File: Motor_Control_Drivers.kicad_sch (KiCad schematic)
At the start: 4 parts, among them J1101 SEI-125-02-GF-S-M-AT, J1102 SEI-115-02-GF-S-M-AT

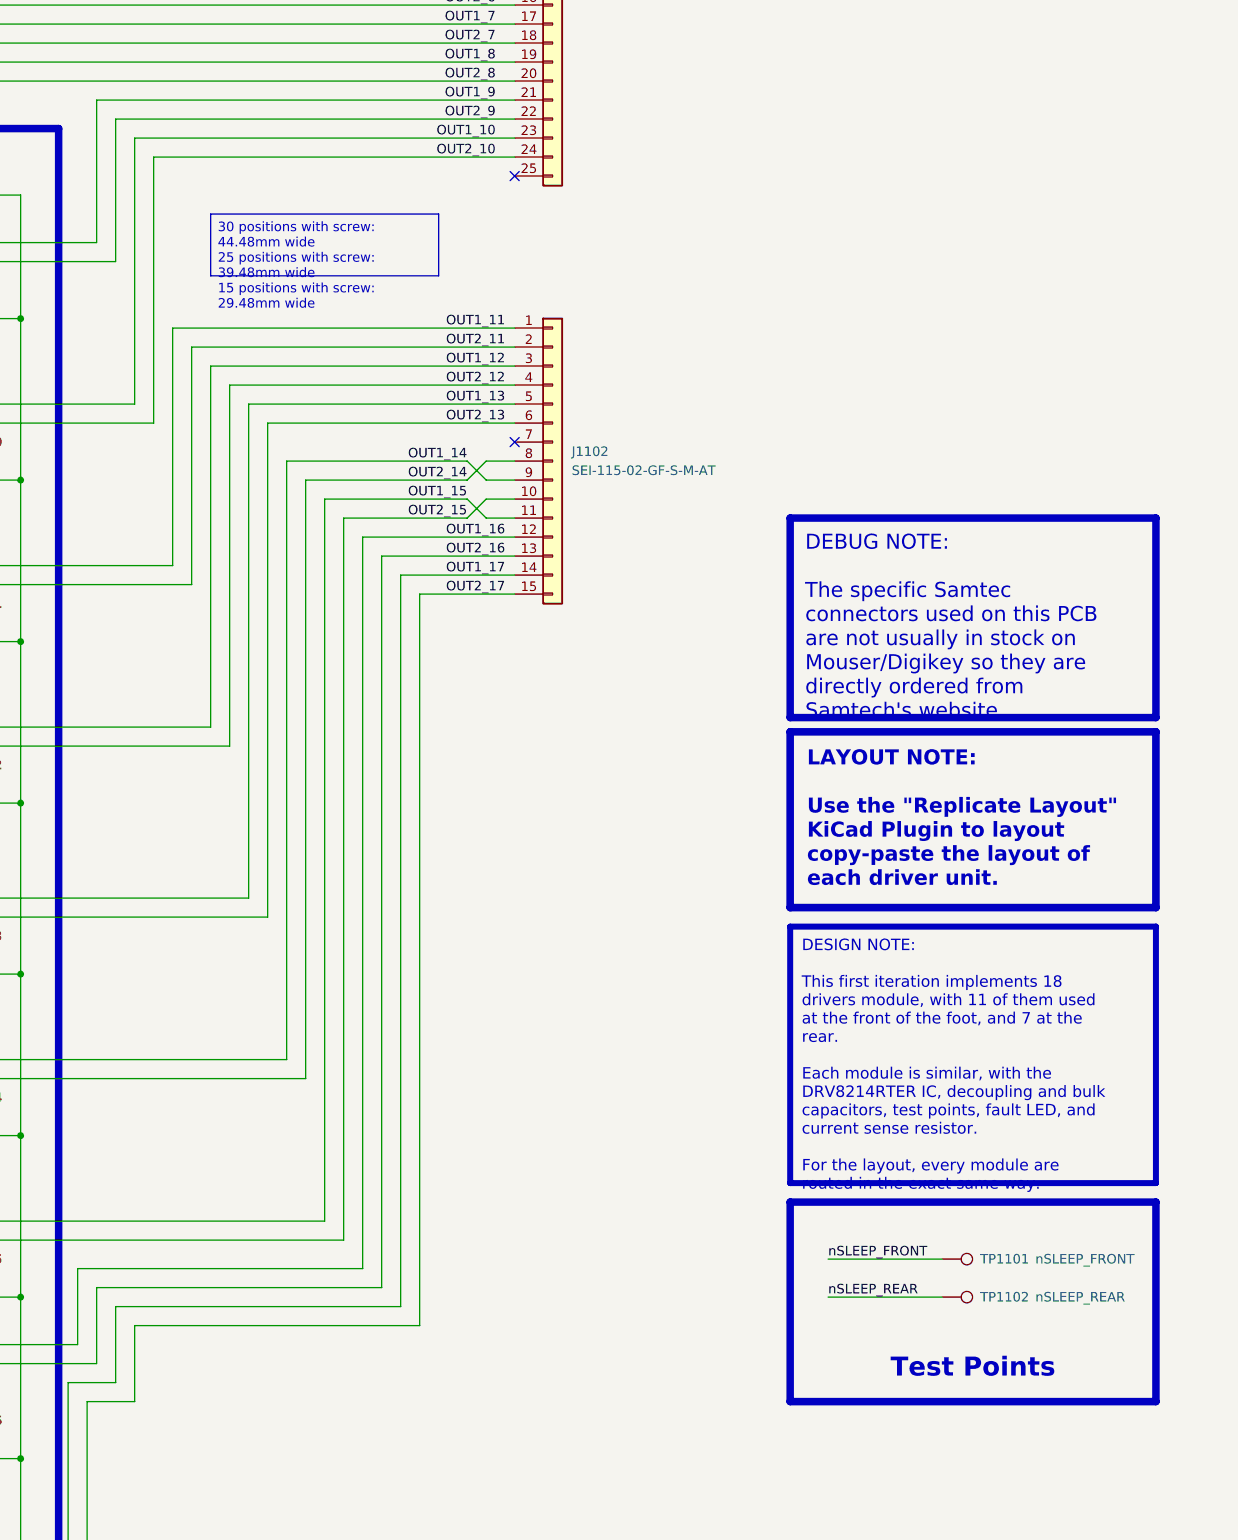
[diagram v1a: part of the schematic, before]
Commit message: Added PCB frame for assembly, almost finished auto-review, only MCU and motors left
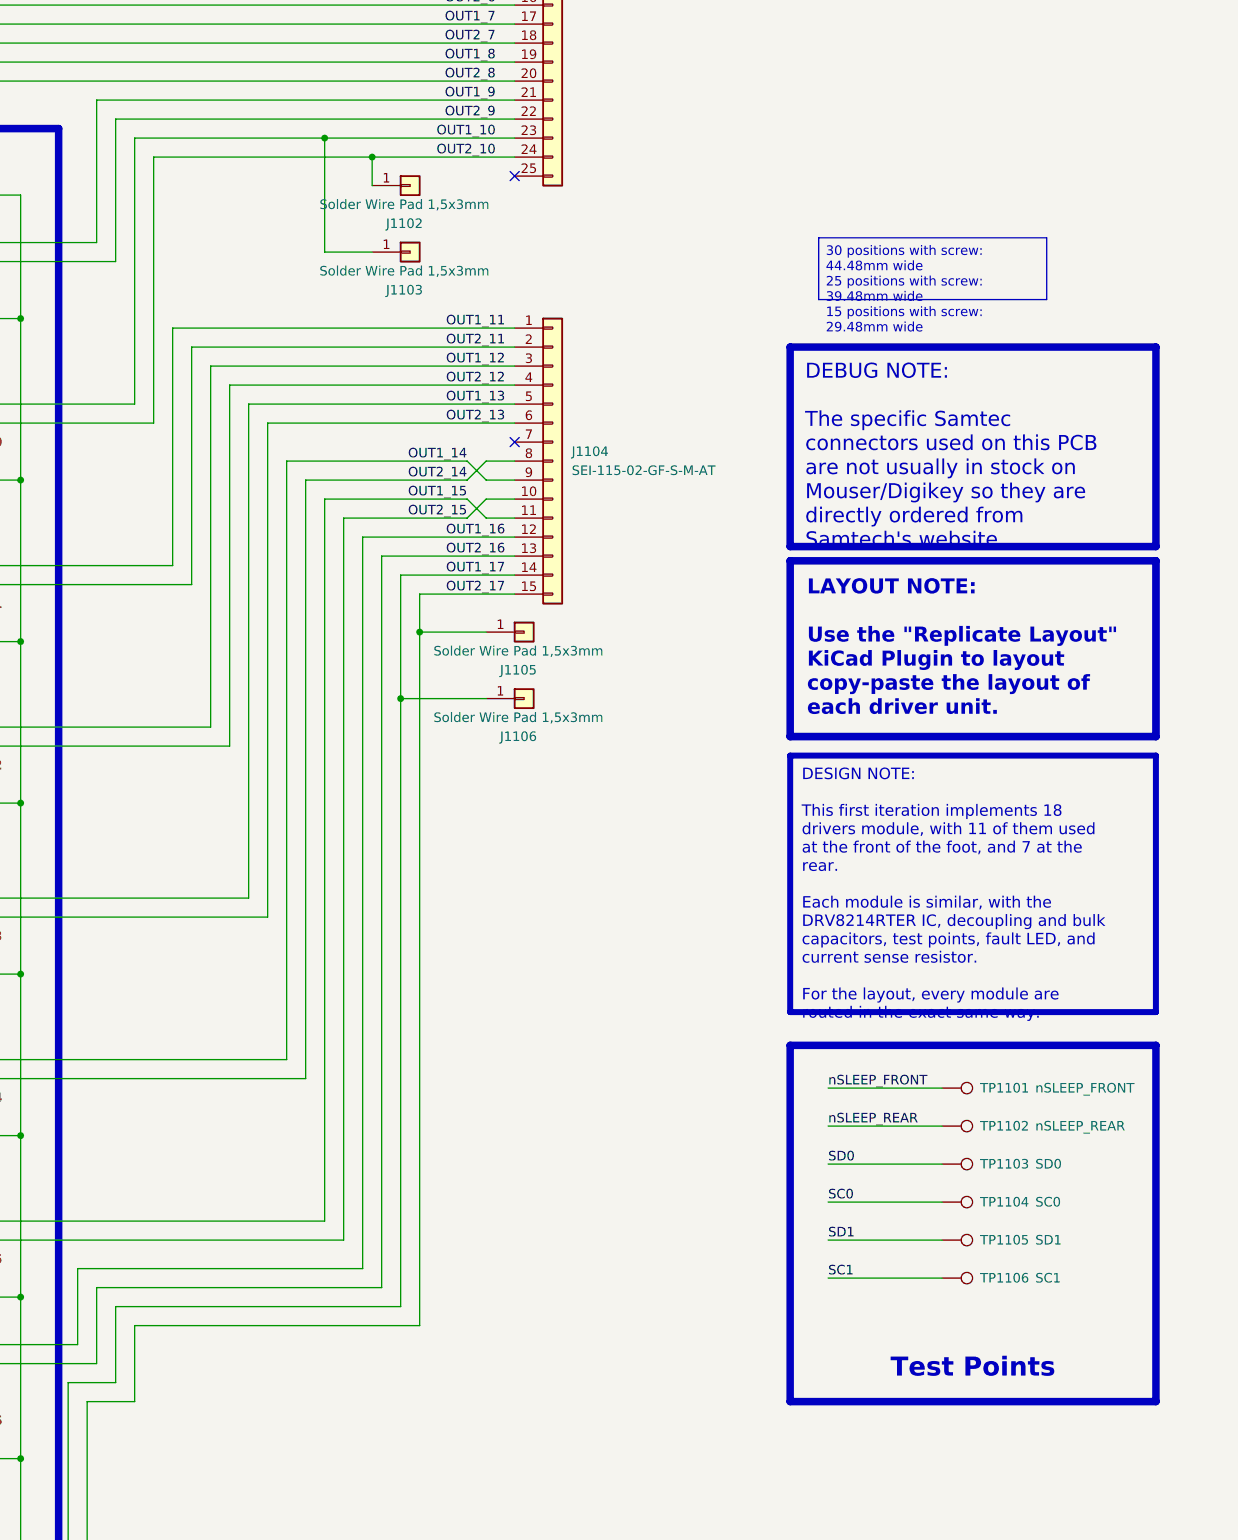
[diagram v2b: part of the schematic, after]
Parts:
- added J1102, J1103, J1105, J1106: Solder Wire Pad 1,5x3mm, 0_Plume:Connector_SolderWirePad_SMD_1,5x3mm, symbol Connector_Generic:Conn_01x01
- added TP1103: SD0, 0_Plume:TestPoint_Pad_D0.75mm_Front, symbol Connector:TestPoint
- added TP1104: SC0, 0_Plume:TestPoint_Pad_D0.75mm_Front, symbol Connector:TestPoint
- added TP1105: SD1, 0_Plume:TestPoint_Pad_D0.75mm_Front, symbol Connector:TestPoint
- added TP1106: SC1, 0_Plume:TestPoint_Pad_D0.75mm_Front, symbol Connector:TestPoint
- renumbered J1102 to J1104
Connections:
- net OUT1_10: now also J1103.1 (Pin_1)
- net OUT1_17: now also J1106.1 (Pin_1)
- net OUT2_10: now also J1102.1 (Pin_1)
- net OUT2_17: now also J1105.1 (Pin_1)
- net SC0: now also TP1104.1
- net SC1: now also TP1106.1
- net SD0: now also TP1103.1
- net SD1: now also TP1105.1
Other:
- moved on the sheet: TP1101, TP1102

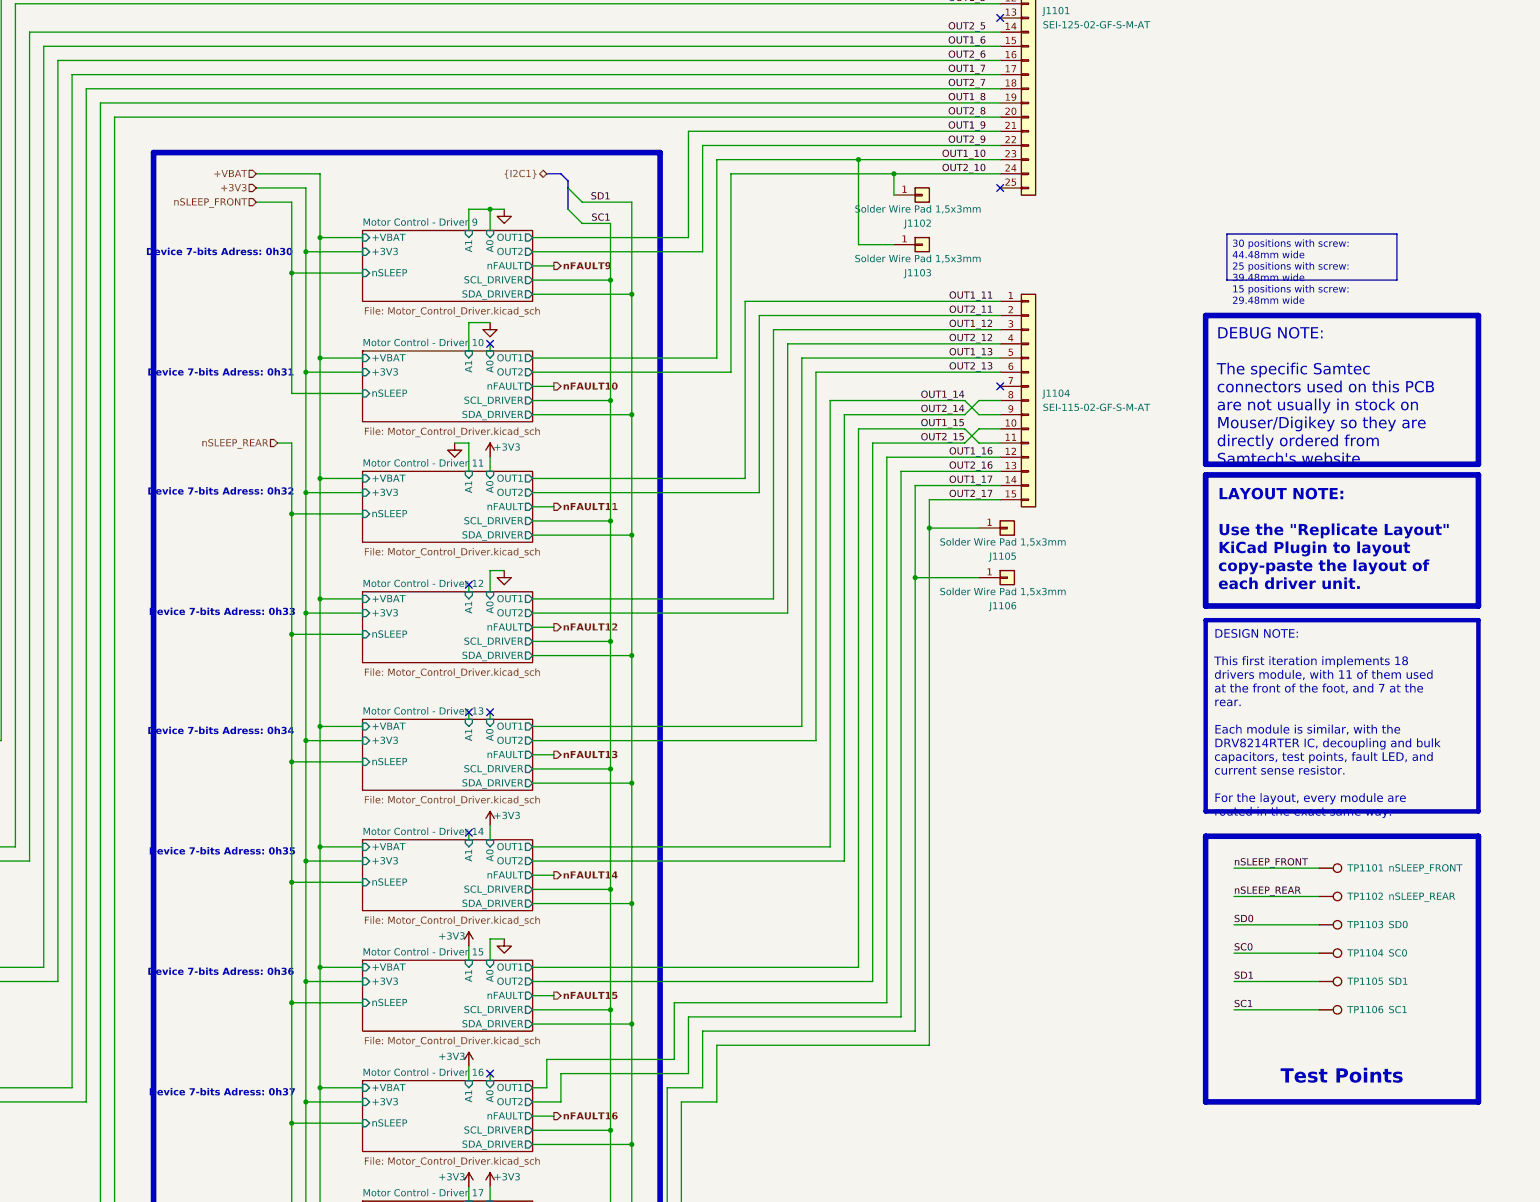
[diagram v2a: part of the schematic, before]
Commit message: Checked everything, corrected footprints, cleaned routing, should be ready to order
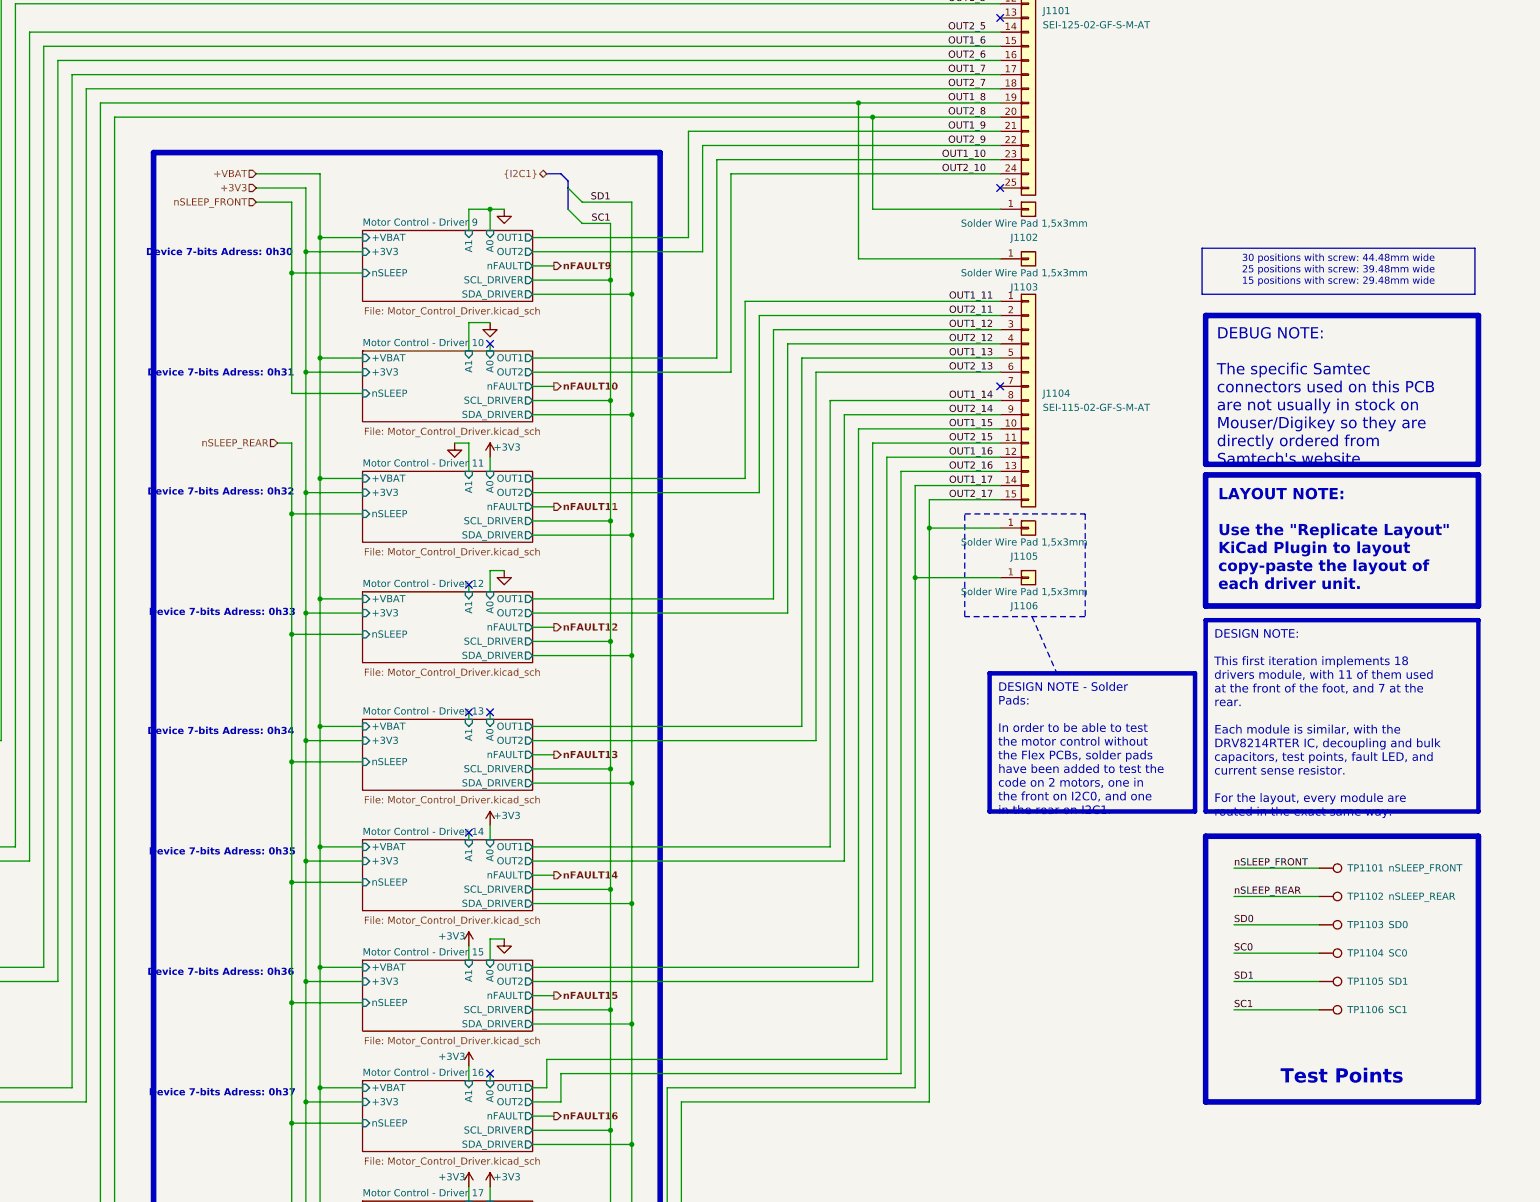
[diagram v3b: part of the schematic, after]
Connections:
- net OUT1_10: no longer J1103.1 (Pin_1)
- net OUT1_14: now also J1104.8 (Pin_8); no longer J1104.9 (Pin_9)
- net OUT1_15: now also J1104.10 (Pin_10); no longer J1104.11 (Pin_11)
- net OUT1_8: now also J1103.1 (Pin_1)
- net OUT2_10: no longer J1102.1 (Pin_1)
- net OUT2_14: now also J1104.9 (Pin_9); no longer J1104.8 (Pin_8)
- net OUT2_15: now also J1104.11 (Pin_11); no longer J1104.10 (Pin_10)
- net OUT2_8: now also J1102.1 (Pin_1)
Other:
- moved on the sheet: J1102, J1103, J1105, J1106
